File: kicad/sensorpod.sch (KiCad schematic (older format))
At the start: 48 parts

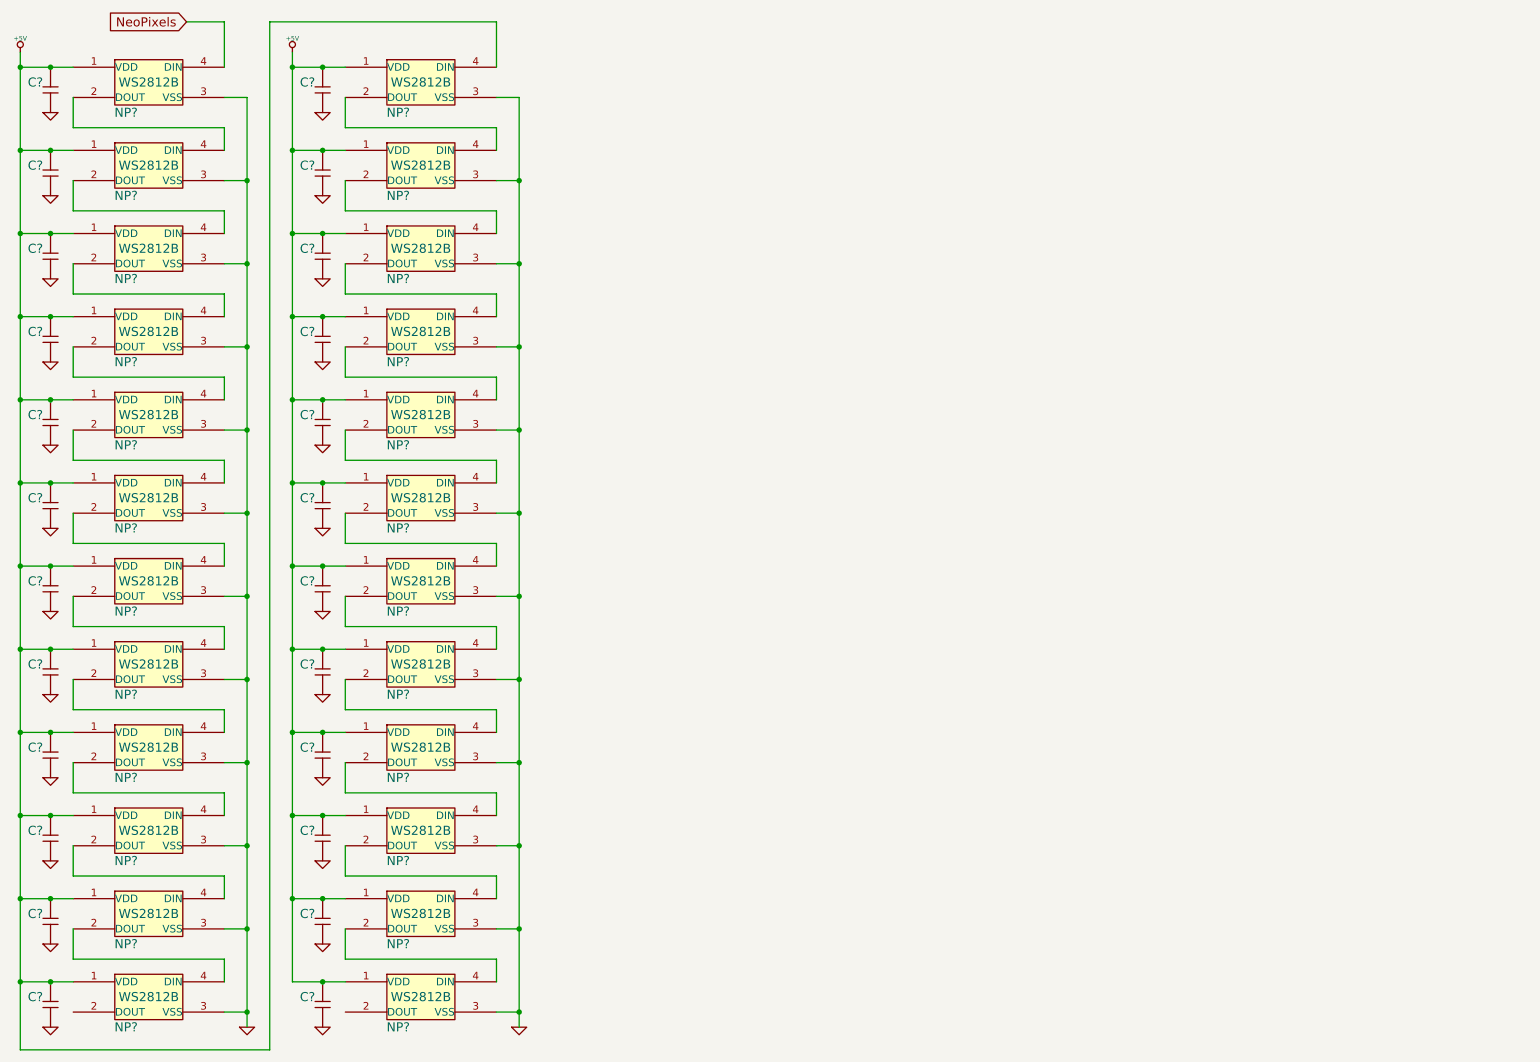
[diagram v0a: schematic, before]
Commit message: Sensor pos schematic done
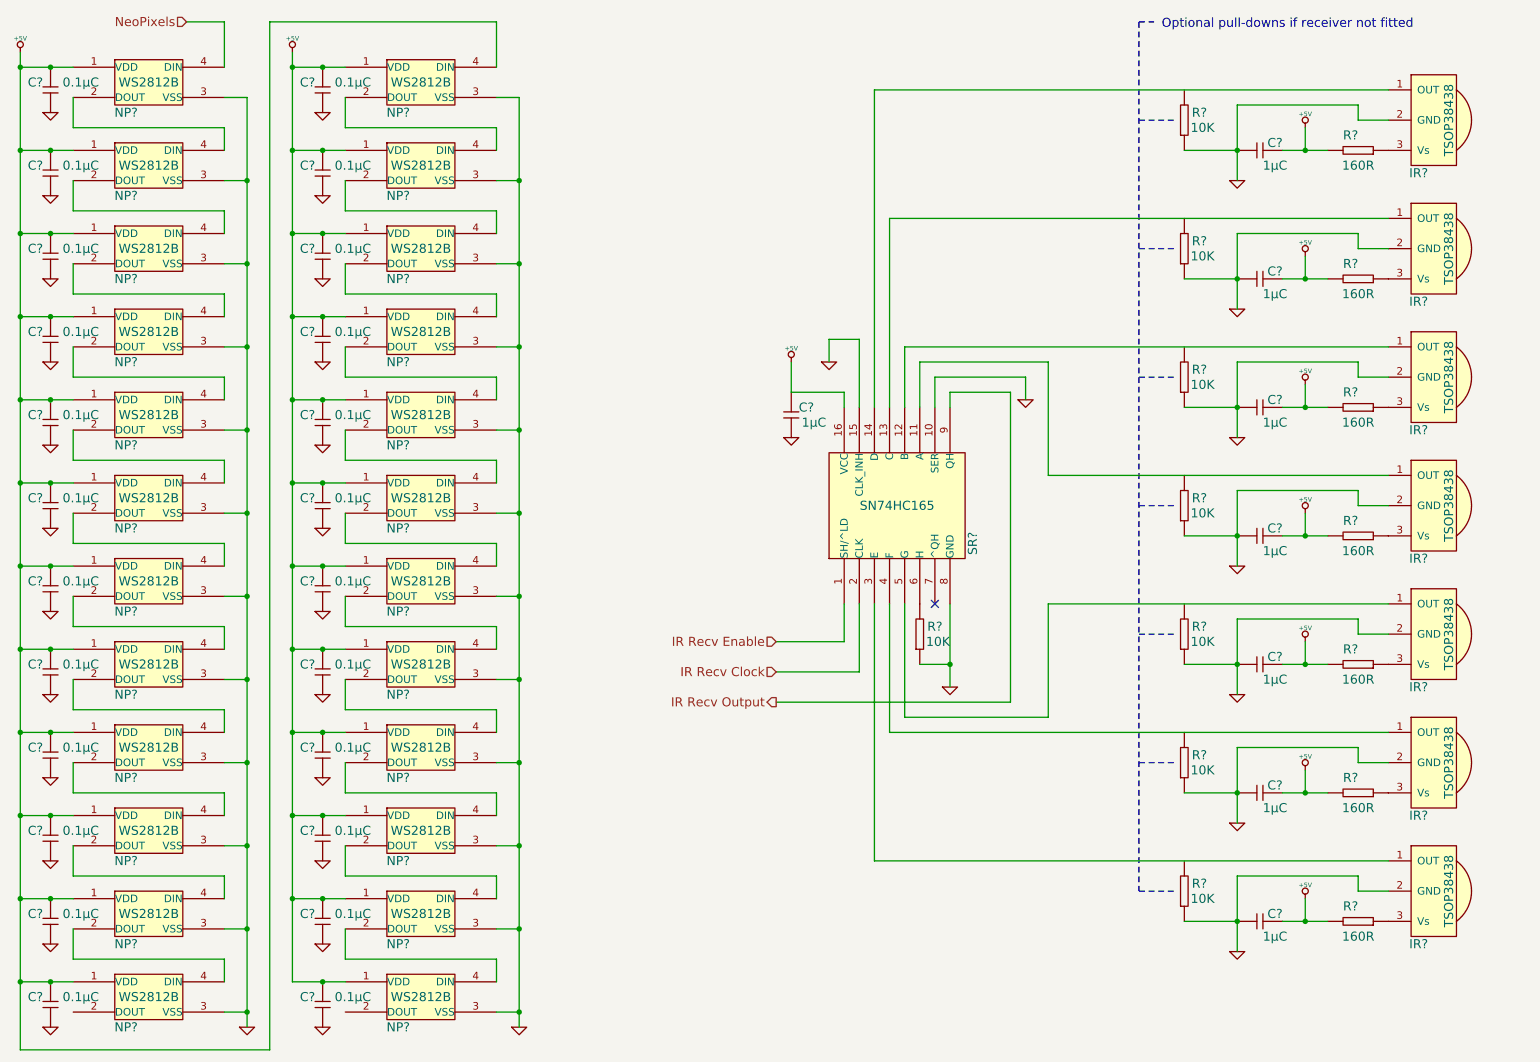
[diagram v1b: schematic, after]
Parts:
- added C? (x8): GENERIC_CAPACITOR, ~, symbol GENERIC_CAPACITOR
- added IR? (x7): TSOP38438, ~, symbol TSOP38438
- added R? (x15): GENERIC_RESISTOR, ~, symbol GENERIC_RESISTOR
- added SR?: SN74HC165, ~, symbol SN74HC165
- C? (x24): Capacitance (none) -> 0.1µC
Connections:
- net +5V: now also C?.1, C?.1, C?.1, C?.1, C?.1, C?.1, C?.1, C?.1, R?.1, R?.1, R?.1, R?.1, R?.1, R?.1, R?.1, SR?.16 (VCC)
- net GND: now also C?.2, C?.2, C?.2, C?.2, C?.2, C?.2, C?.2, C?.2, IR?.2 (GND), IR?.2 (GND), IR?.2 (GND), IR?.2 (GND), IR?.2 (GND), IR?.2 (GND), IR?.2 (GND), R?.2, R?.2, R?.2, R?.2, R?.2, R?.2, R?.2, R?.2, SR?.10 (SER), SR?.15 (CLK_INH), SR?.8 (GND)
- new net: R?.1, SR?.6 (H)
- new net: IR?.3 (Vs), R?.2 (x7)
- new net: IR?.1 (OUT), SR?.11 (A)
- new net: IR?.1 (OUT), SR?.12 (B)
- new net: IR?.1 (OUT), SR?.13 (C)
- new net: IR?.1 (OUT), SR?.14 (D)
- new net: IR?.1 (OUT), SR?.3 (E)
- new net: IR?.1 (OUT), SR?.4 (F)
- new net: IR?.1 (OUT), SR?.5 (G)
- new net IR Recv Clock: SR?.2 (CLK)
- new net IR Recv Enable: SR?.1 (SH/^LD)
- new net IR Recv Output: SR?.9 (QH)
- no-connect marks 0 -> 1
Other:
- note added: "Optional pull-downs if receiver not fitted"
